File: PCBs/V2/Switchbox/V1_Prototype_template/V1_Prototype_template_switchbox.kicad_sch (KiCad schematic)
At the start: 7 parts

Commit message: some progress on switchbox schematic
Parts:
- added J1, J2: Conn_02x10_Top_Bottom, Connector_PinHeader_1.00mm:PinHeader_2x10_P1.00mm_Vertical, symbol Connector_Generic:Conn_02x10_Top_Bottom
- renumbered UART1(COMS) to UART1(COMS)1
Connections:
- net GND: now also J2.1 (Pin_1), J2.10 (Pin_10), J2.11 (Pin_11), J2.12 (Pin_12), J2.13 (Pin_13), J2.14 (Pin_14), J2.15 (Pin_15), J2.16 (Pin_16), J2.17 (Pin_17), J2.18 (Pin_18), J2.19 (Pin_19), J2.2 (Pin_2), J2.20 (Pin_20), J2.3 (Pin_3), J2.4 (Pin_4), J2.5 (Pin_5), J2.6 (Pin_6), J2.7 (Pin_7), J2.8 (Pin_8), J2.9 (Pin_9)
- net PA0: now also J1.1 (Pin_1)
- net SWCLK: no longer STM32L031K6Tx1.23 (PA13)
- net SWDIO: no longer STM32L031K6Tx1.24 (PA14)
- net PB0: now reaches STM32L031K6Tx1.14 (PB0)
- net PB0: now also J1.13 (Pin_13)
- net PB1: now reaches STM32L031K6Tx1.15 (PB1)
- net PB1: now also J1.14 (Pin_14)
- net PA8: now reaches STM32L031K6Tx1.18 (PA8)
- net PA8: now also J1.9 (Pin_9)
- net PC14: now reaches STM32L031K6Tx1.2 (PC14)
- net PB3: now reaches STM32L031K6Tx1.26 (PB3)
- net PB3: now also J1.15 (Pin_15)
- net PB4: now reaches STM32L031K6Tx1.27 (PB4)
- net PB4: now also J1.16 (Pin_16)
- net PB5: now reaches STM32L031K6Tx1.28 (PB5)
- net PB5: now also J1.17 (Pin_17)
- net PB6: now reaches STM32L031K6Tx1.29 (PB6)
- net PB6: now also J1.18 (Pin_18)
- net PC15: now reaches STM32L031K6Tx1.3 (PC15)
- net PB7: now reaches STM32L031K6Tx1.30 (PB7)
- net PB7: now also J1.19 (Pin_19)
- net PA1: now reaches STM32L031K6Tx1.7 (PA1)
- net PA1: now also J1.2 (Pin_2)
- net PA2: now reaches STM32L031K6Tx1.8 (PA2)
- net PA2: now also J1.3 (Pin_3)
- net PA3: now reaches STM32L031K6Tx1.9 (PA3)
- net PA3: now also J1.4 (Pin_4)
- net IN_0 renamed PA11
- net PA11: now also J1.10 (Pin_10)
- net IN_1 renamed PA12
- net PA12: now also J1.11 (Pin_11)
- net IN_2 renamed PA15
- net PA15: now also J1.12 (Pin_12)
- net S0 renamed PA4
- net PA4: now also J1.5 (Pin_5)
- net S1 renamed PA5
- net PA5: now also J1.6 (Pin_6)
- net S2 renamed PA6
- net PA6: now also J1.7 (Pin_7)
- net S3 renamed PA7
- net PA7: now also J1.8 (Pin_8)
- net UART_RX renamed UART_RX(PA10)
- net UART_TX renamed UART_TX(PA9)
- new net SWCLK(PA13): STM32L031K6Tx1.23 (PA13)
- new net SWDIO(PA14): STM32L031K6Tx1.24 (PA14)
- no-connect marks 13 -> 1
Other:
- moved on the sheet: 1k1, 1k2, Leave_Open1, Reset1

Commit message: progress on switchboard schematic
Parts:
- added J3(IN)1, J5(OUT)1: 5360, FootprintLibrary:5360, symbol 5360:5360
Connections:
- net GND: now also J3(IN)1.3, J5(OUT)1.3; no longer J2.11 (Pin_11), J2.12 (Pin_12), J2.13 (Pin_13), J2.14 (Pin_14), J2.15 (Pin_15), J2.16 (Pin_16), J2.17 (Pin_17), J2.18 (Pin_18), J2.19 (Pin_19), J2.20 (Pin_20)
- net UART_RX(PA10): now also J3(IN)1.1, J5(OUT)1.2
- net UART_TX(PA9): now also J3(IN)1.2, J5(OUT)1.1
- net VCC: now also J2.11 (Pin_11), J2.12 (Pin_12), J2.13 (Pin_13), J2.14 (Pin_14), J2.15 (Pin_15), J2.16 (Pin_16), J2.17 (Pin_17), J2.18 (Pin_18), J2.19 (Pin_19), J2.20 (Pin_20)
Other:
- note added: "IN"
- note added: "OUT"
- note added: "Through hole ferruels or solder cups"
- moved on the sheet: Programmer1

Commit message: good progress on switchbox pcb design
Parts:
- removed J3(IN)1, J5(OUT)1: 5360, FootprintLibrary:5360, symbol 5360:5360
- removed UART1(COMS)1: Conn_01x02_Pin, Connector_PinHeader_2.54mm:PinHeader_1x02_P2.54mm_Vertical, symbol Connector:Conn_01x02_Pin
- added J3: Conn_02x10_Top_Bottom, Connector_PinHeader_1.00mm:PinHeader_2x10_P1.00mm_Vertical, symbol Connector_Generic:Conn_02x10_Top_Bottom
- added J3(IN)1, J5(OUT)1: 01x04 magnetic connector, FootprintLibrary:5358_4pin_connector_customfootprint, symbol Connector_Generic:Conn_01x04
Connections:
- net GND: now also J2.11 (Pin_11), J2.12 (Pin_12), J2.13 (Pin_13), J2.14 (Pin_14), J2.15 (Pin_15), J2.16 (Pin_16), J2.17 (Pin_17), J2.18 (Pin_18), J2.19 (Pin_19), J2.20 (Pin_20), J3(IN)1.1 (Pin_1), J5(OUT)1.1 (Pin_1)
- net UART_RX(PA10): now also J3(IN)1.4 (Pin_4), J5(OUT)1.3 (Pin_3)
- net UART_TX(PA9): now also J3(IN)1.3 (Pin_3), J5(OUT)1.4 (Pin_4)
- net VCC: now also J3(IN)1.2 (Pin_2), J3.1 (Pin_1), J3.10 (Pin_10), J3.11 (Pin_11), J3.12 (Pin_12), J3.13 (Pin_13), J3.14 (Pin_14), J3.15 (Pin_15), J3.16 (Pin_16), J3.17 (Pin_17), J3.18 (Pin_18), J3.19 (Pin_19), J3.2 (Pin_2), J3.20 (Pin_20), J3.3 (Pin_3), J3.4 (Pin_4), J3.5 (Pin_5), J3.6 (Pin_6), J3.7 (Pin_7), J3.8 (Pin_8), J3.9 (Pin_9), J5(OUT)1.2 (Pin_2); no longer J2.11 (Pin_11), J2.12 (Pin_12), J2.13 (Pin_13), J2.14 (Pin_14), J2.15 (Pin_15), J2.16 (Pin_16), J2.17 (Pin_17), J2.18 (Pin_18), J2.19 (Pin_19), J2.20 (Pin_20)

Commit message: PCB For switchbox prototype done
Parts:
- removed J1, J2, J3: Conn_02x10_Top_Bottom, Connector_PinHeader_1.00mm:PinHeader_2x10_P1.00mm_Vertical, symbol Connector_Generic:Conn_02x10_Top_Bottom
- added U1: ~, FootprintLibrary:PinHeader_03x20, symbol Switchbox_symbols:PinHeader_03x20
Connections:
- net GND: now also J5(OUT)1.4 (Pin_4), U1.1, U1.10, U1.13, U1.16, U1.19, U1.22, U1.25, U1.28, U1.31, U1.34, U1.37, U1.4, U1.40, U1.43, U1.46, U1.49, U1.52, U1.55, U1.58, U1.7; no longer J5(OUT)1.1 (Pin_1)
- net PA0: now also U1.33
- net PA1: now also U1.36
- net PA11: now also U1.27
- net PA12: now also U1.24
- net PA15: now also U1.21
- net PA2: now also U1.39
- net PA3: now also U1.42
- net PA4: now also U1.45
- net PA5: now also U1.48
- net PA6: now also U1.51
- net PA7: now also U1.54
- net PA8: now also U1.30
- net PB0: now also U1.57
- net PB1: now also U1.60
- net PB3: now also U1.18
- net PB4: now also U1.15
- net PB5: now also U1.12
- net PB6: now also U1.9
- net PB7: now also U1.6
- net UART_RX(PA10): now also J5(OUT)1.2 (Pin_2); no longer J5(OUT)1.3 (Pin_3)
- net UART_TX(PA9): now also J5(OUT)1.1 (Pin_1); no longer J5(OUT)1.4 (Pin_4)
- net VCC: now also J5(OUT)1.3 (Pin_3), U1.11, U1.14, U1.17, U1.2, U1.20, U1.23, U1.26, U1.29, U1.32, U1.35, U1.38, U1.41, U1.44, U1.47, U1.5, U1.50, U1.53, U1.56, U1.59, U1.8; no longer J5(OUT)1.2 (Pin_2)
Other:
- note added: "This connector is layed out like a 3x20 servo header. Through hole ferruels or solder cups OR standard servo headers"
- note removed: "Through hole ferruels or solder cups"
- moved on the sheet: J5(OUT)1

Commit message: small fixes to switchbox pcb
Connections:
- net SWCLK(PA13) is gone; now on net SWDIO(PA13): STM32L031K6Tx1.23 (PA13)
- net SWDIO(PA14) is gone; now on net SWCLK(PA14): STM32L031K6Tx1.24 (PA14)
- net SWCLK renamed SWDIO(PA13)
- net SWDIO renamed SWCLK(PA14)
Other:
- note added: "Correct order swdio swclk to match misnaming in some other projects"
- note added: "Note, in some of these schematics sclck and sdio mislabeled, this is correct here"
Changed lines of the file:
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@@
 	(generator_version "9.0")
 	(paper "A4")
+	(text "Note, in some of these schematics sclck and sdio mislabeled, this is correct here\n"
+		(exclude_from_sim no)
+		(at 180.34 80.264 0)
+		(effects
+			(font
+				(size 1.27 1.27)
+			)
+		)
+	)
 	(text "This connector is layed out like a 3x20 servo header. Through hole ferruels or solder cups OR standard servo headers"
 		(exclude_from_sim no)
@@
 		(exclude_from_sim no)
 		(at 54.864 91.186 0)
+		(effects
+			(font
+				(size 1.27 1.27)
+			)
+		)
+	)
+	(text "Correct order swdio swclk to match misnaming in some other projects\n"
+		(exclude_from_sim no)
+		(at 49.276 60.452 0)
 		(effects
 			(font
@@
 		)
 	)
+	(label "SWDIO(PA13)"
+		(at 57.15 64.77 180)
+		(effects
+			(font
+				(size 1.27 1.27)
+			)
+			(justify right bottom)
+		)
+	)
 	(label "PB3"
 		(at 165.1 58.42 180)
@@
 		)
 	)
-	(label "SWCLK(PA13)"
+	(label "SWDIO(PA13)"
 		(at 125.73 80.01 0)
 		(effects
@@
 		)
 	)
-	(label "SWDIO(PA14)"
+	(label "SWCLK(PA14)"
 		(at 125.73 82.55 0)
 		(effects
@@
 		)
 	)
-	(label "SWCLK"
-		(at 57.15 64.77 180)
-		(effects
-			(font
-				(size 1.27 1.27)
-			)
-			(justify right bottom)
-		)
-	)
 	(label "PC14"
 		(at 95.25 57.15 180)
@@
 		)
 	)
+	(label "SWCLK(PA14)"
+		(at 57.15 67.31 180)
+		(effects
+			(font
+				(size 1.27 1.27)
+			)
+			(justify right bottom)
+		)
+	)
 	(label "PA5"
 		(at 125.73 59.69 0)
@@
 		)
 	)
-	(label "SWDIO"
-		(at 57.15 67.31 180)
-		(effects
-			(font
-				(size 1.27 1.27)
-			)
-			(justify right bottom)
-		)
-	)

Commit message: some updates
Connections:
- net UART_RX(PA10) renamed USART_RX(PA10)
- net UART_TX(PA9) renamed USART_TX(PA9)
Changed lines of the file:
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@@
 		)
 	)
-	(label "UART_TX(PA9)"
+	(label "USART_TX(PA9)"
 		(at 72.39 104.14 180)
 		(effects
@@
 		)
 	)
-	(label "UART_RX(PA10)"
+	(label "USART_RX(PA10)"
 		(at 82.55 91.44 0)
 		(effects
@@
 		)
 	)
-	(label "UART_TX(PA9)"
+	(label "USART_TX(PA9)"
 		(at 125.73 69.85 0)
 		(effects
@@
 		)
 	)
-	(label "UART_RX(PA10)"
+	(label "USART_RX(PA10)"
 		(at 72.39 106.68 180)
 		(effects
@@
 		)
 	)
-	(label "UART_RX(PA10)"
+	(label "USART_RX(PA10)"
 		(at 125.73 72.39 0)
 		(effects
@@
 		)
 	)
-	(label "UART_TX(PA9)"
+	(label "USART_TX(PA9)"
 		(at 82.55 93.98 0)
 		(effects

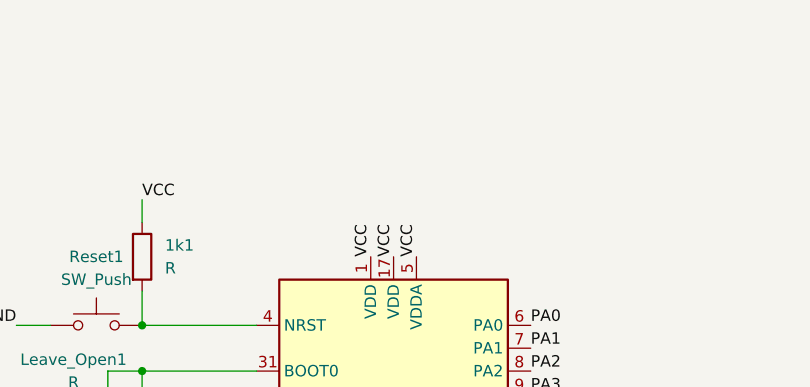
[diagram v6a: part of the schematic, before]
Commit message: messed UART connection for synthesis PCB :/ good thing i had those misc pads for testing. Need to reorder.
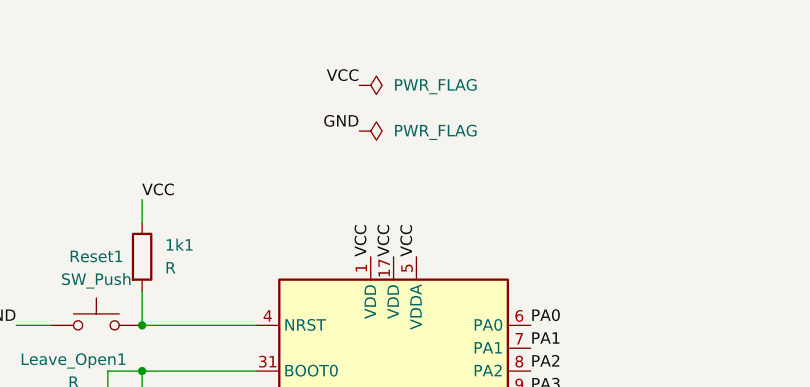
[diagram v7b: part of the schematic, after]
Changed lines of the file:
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@@
+	)
+	(label "GND"
+		(at 106.68 25.4 180)
+		(effects
+			(font
+				(size 1.27 1.27)
+			)
+			(justify right bottom)
+		)
 	)
 	(label "GND"
@@
 	(label "USART_RX(PA10)"
 		(at 72.39 106.68 180)
+		(effects
+			(font
+				(size 1.27 1.27)
+			)
+			(justify right bottom)
+		)
+	)
+	(label "VCC"
+		(at 106.68 20.32 180)
 		(effects
 			(font
@@
 					(unit 1)
 				)
+			)
+		)
+	)
+	(symbol
+		(lib_id "power:PWR_FLAG")
+		(at 106.68 20.32 270)
+		(unit 1)
+		(exclude_from_sim no)
+		(in_bom yes)
+		(on_board yes)
+		(dnp no)
+		(fields_autoplaced yes)
+		(property "Reference" "#FLG01"
+			(at 108.585 20.32 0)
+			(effects
+				(font
+					(size 1.27 1.27)
+				)
+				(hide yes)
+			)
+		)
+		(property "Value" "PWR_FLAG"
+			(at 110.49 20.3199 90)
+			(effects
+				(font
+					(size 1.27 1.27)
+				)
+				(justify left)
+			)
+		)
+		(property "Footprint" ""
+			(at 106.68 20.32 0)
+			(effects
+				(font
+					(size 1.27 1.27)
+				)
+				(hide yes)
+			)
+		)
+		(property "Datasheet" "~"
+			(at 106.68 20.32 0)
+			(effects
+				(font
+					(size 1.27 1.27)
+				)
+				(hide yes)
+			)
+		)
+		(property "Description" "Special symbol for telling ERC where power comes from"
+			(at 106.68 20.32 0)
+			(effects
+				(font
+					(size 1.27 1.27)
+				)
+				(hide yes)
+			)
+		)
+		(pin "1"
+		)
+		(instances
+			(project ""
+				(path "/fa4be861-32fe-46a0-bf45-cacc0f983074"
+					(reference "#FLG01")
+					(unit 1)
+				)
+			)
+		)
+	)
+	(symbol
+		(lib_id "power:PWR_FLAG")
+		(at 106.68 25.4 270)
+		(unit 1)
+		(exclude_from_sim no)
+		(in_bom yes)
+		(on_board yes)
+		(dnp no)
+		(fields_autoplaced yes)
+		(property "Reference" "#FLG02"
+			(at 108.585 25.4 0)
+			(effects
+				(font
+					(size 1.27 1.27)
+				)
+				(hide yes)
+			)
+		)
+		(property "Value" "PWR_FLAG"
+			(at 110.49 25.3999 90)
+			(effects
+				(font
+					(size 1.27 1.27)
+				)
+				(justify left)
+			)
+		)
+		(property "Footprint" ""
+			(at 106.68 25.4 0)
+			(effects
+				(font
+					(size 1.27 1.27)
+				)
+				(hide yes)
+			)
+		)
+		(property "Datasheet" "~"
+			(at 106.68 25.4 0)
+			(effects
+				(font
+					(size 1.27 1.27)
+				)
+				(hide yes)
+			)
+		)
+		(property "Description" "Special symbol for telling ERC where power comes from"
+			(at 106.68 25.4 0)
+			(effects
+				(font
+					(size 1.27 1.27)
+				)
+				(hide yes)
+			)
+		)
+		(pin "1"
+		)
+		(instances
+			(project "V1_Prototype_template_switchbox"
+				(path "/fa4be861-32fe-46a0-bf45-cacc0f983074"
+					(reference "#FLG02")
+					(unit 1)
+				)

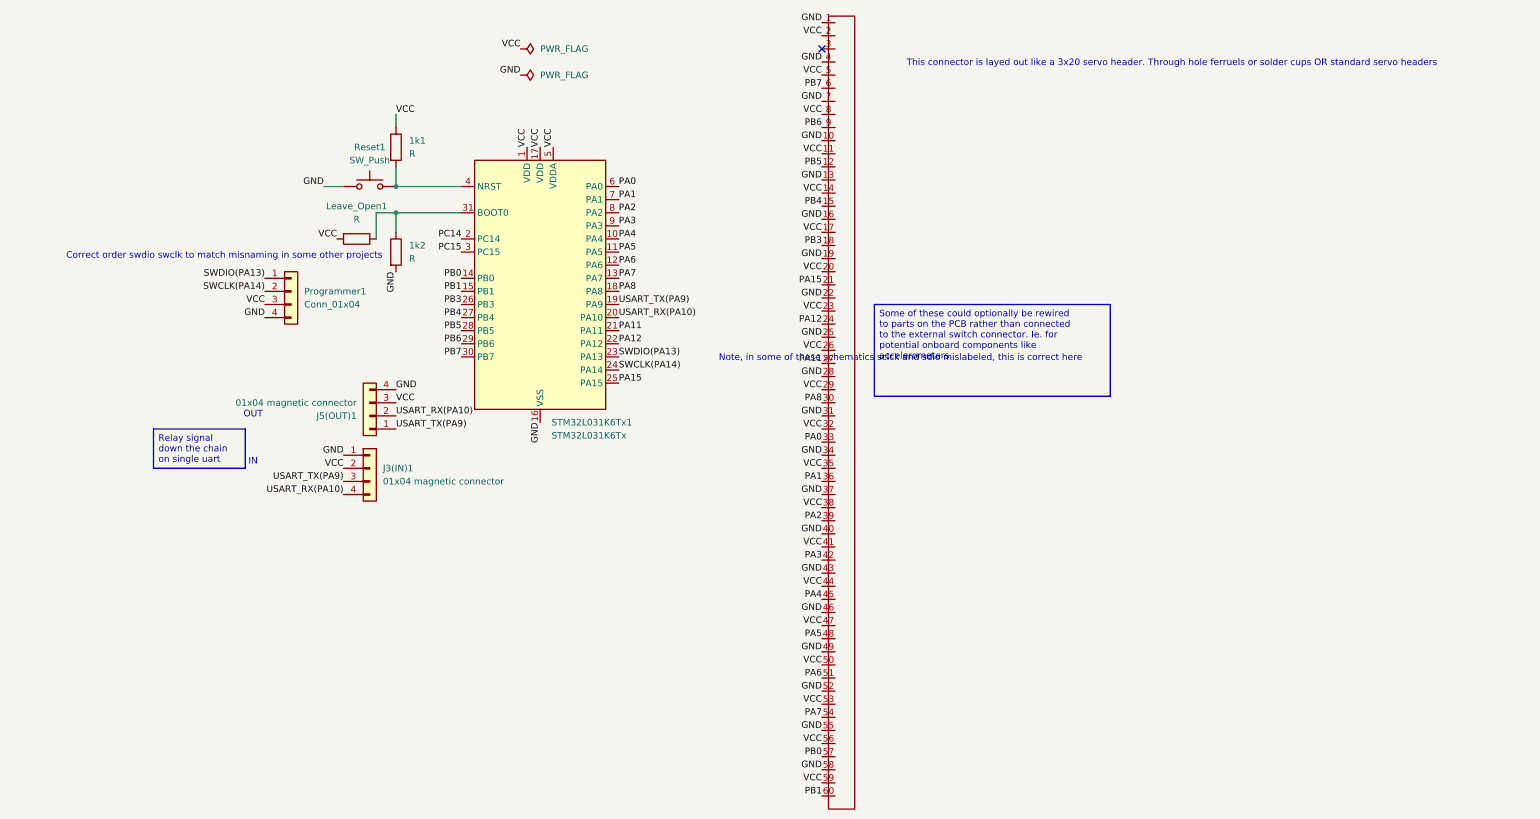
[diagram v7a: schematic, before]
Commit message: Switchbox pcb was also fucked up, fixed that, need to order now. (and tweaked the switchbox boilerplate code.
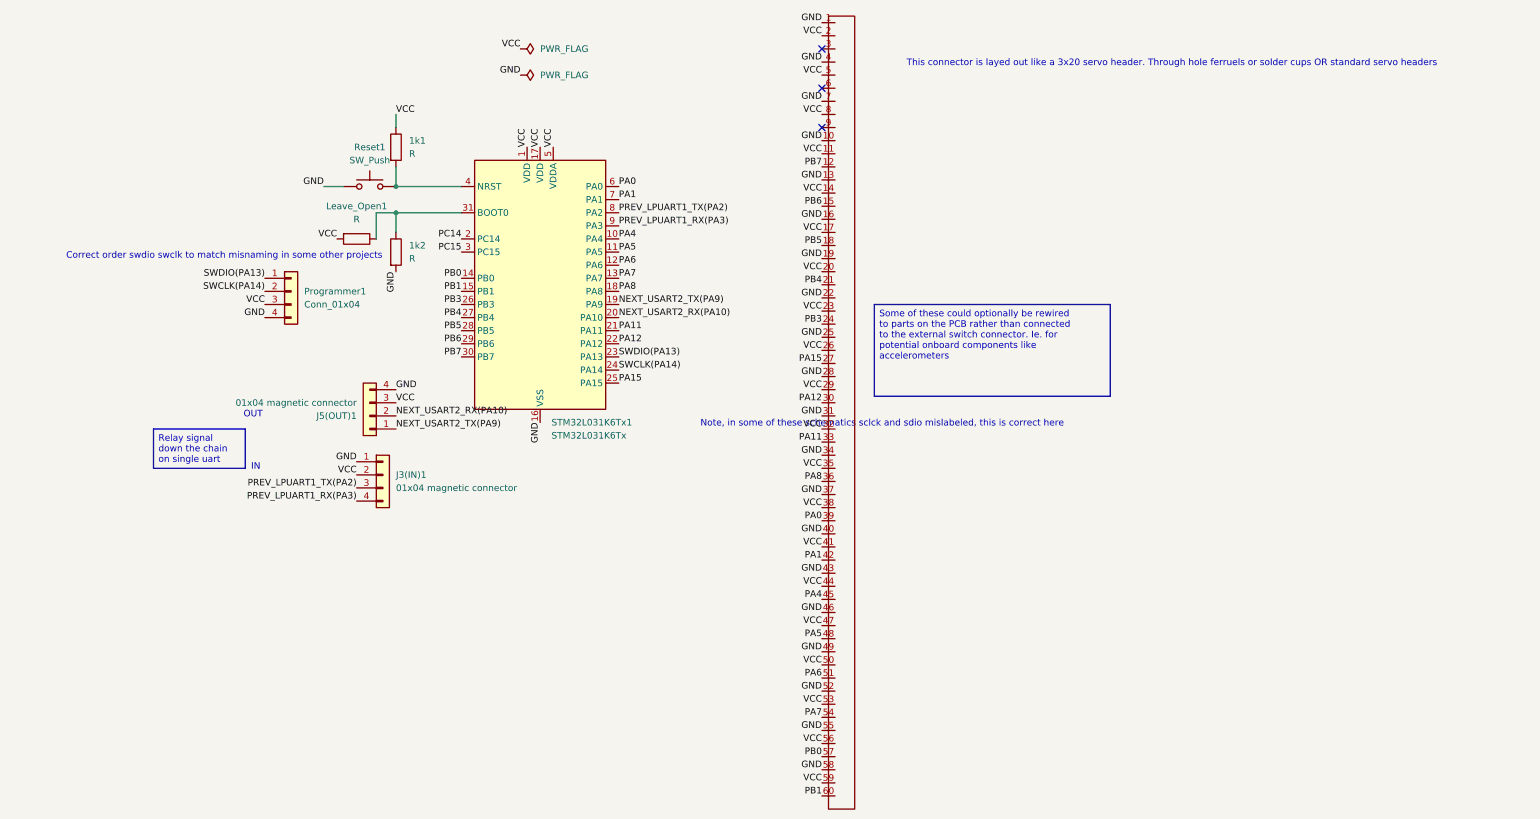
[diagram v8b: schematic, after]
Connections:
- net PA0: now also U1.39; no longer U1.33
- net PA1: now also U1.42; no longer U1.36
- net PA11: now also U1.33; no longer U1.27
- net PA12: now also U1.30; no longer U1.24
- net PA15: now also U1.27; no longer U1.21
- net PA8: now also U1.36; no longer U1.30
- net PB3: now also U1.24; no longer U1.18
- net PB4: now also U1.21; no longer U1.15
- net PB5: now also U1.18; no longer U1.12
- net PB6: now also U1.15; no longer U1.9
- net PB7: now also U1.12; no longer U1.6
- net PA2 renamed PREV_LPUART1_TX(PA2)
- net PREV_LPUART1_TX(PA2): now also J3(IN)1.3 (Pin_3); no longer U1.39
- net PA3 renamed PREV_LPUART1_RX(PA3)
- net PREV_LPUART1_RX(PA3): now also J3(IN)1.4 (Pin_4); no longer U1.42
- net USART_RX(PA10) renamed NEXT_USART2_RX(PA10)
- net NEXT_USART2_RX(PA10): no longer J3(IN)1.4 (Pin_4)
- net USART_TX(PA9) renamed NEXT_USART2_TX(PA9)
- net NEXT_USART2_TX(PA9): no longer J3(IN)1.3 (Pin_3)
- no-connect marks 1 -> 3
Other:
- moved on the sheet: J3(IN)1
